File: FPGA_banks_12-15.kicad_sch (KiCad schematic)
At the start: 1 part, among them U1 XC7K410T-2FFG900I

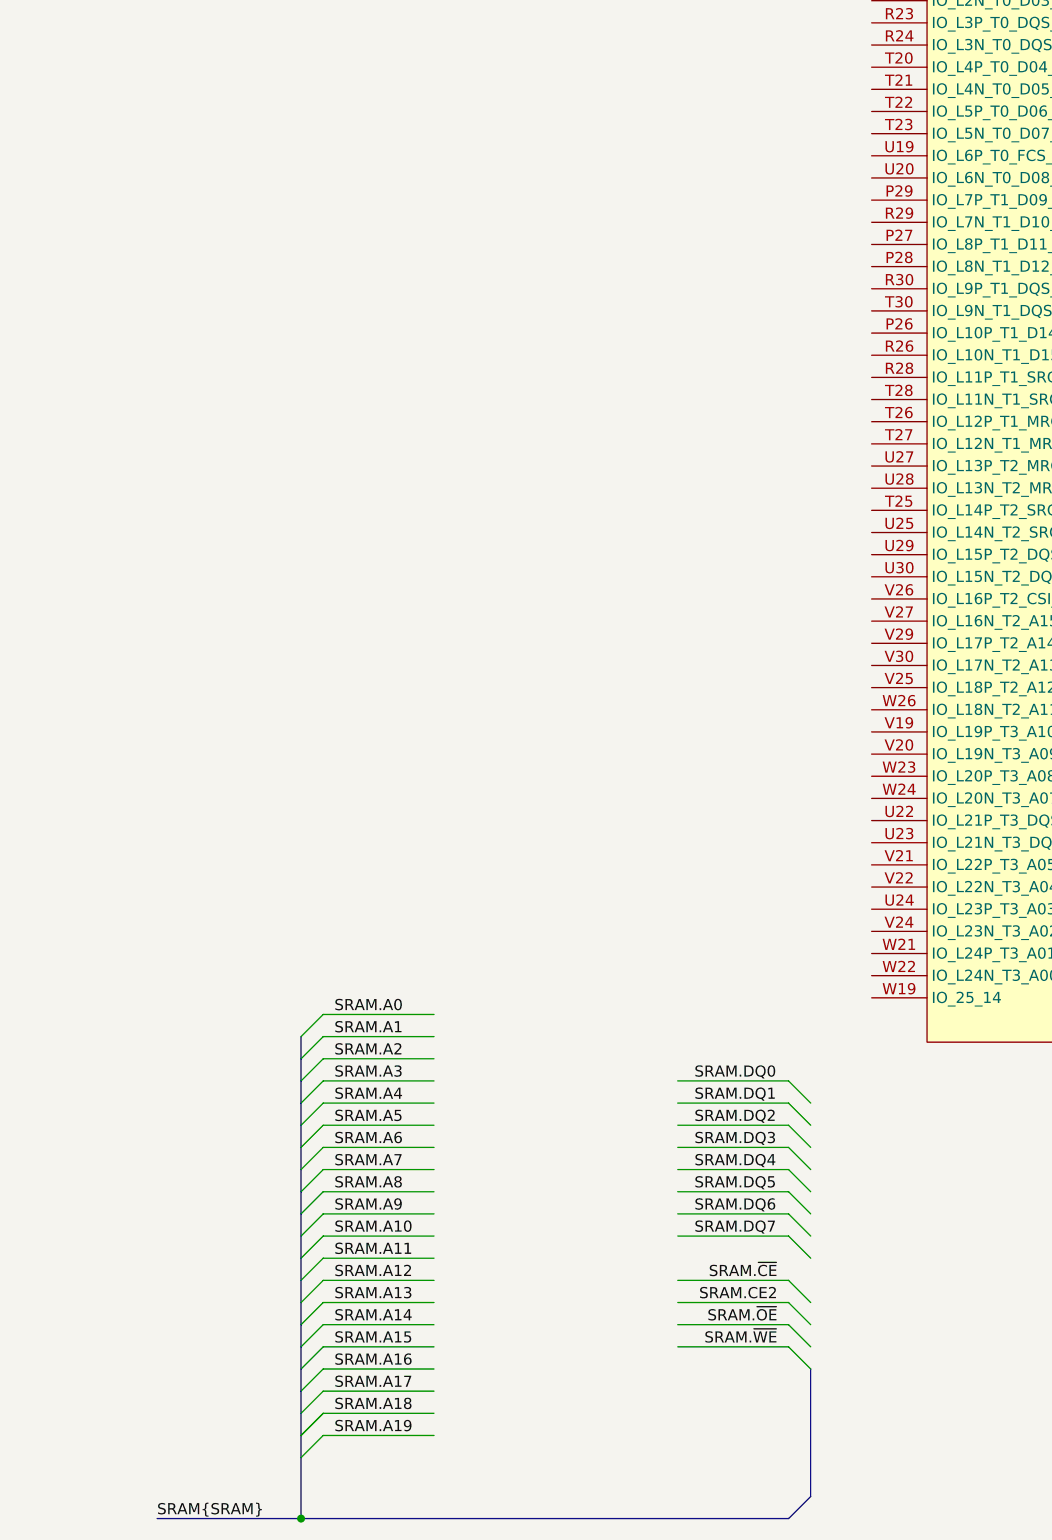
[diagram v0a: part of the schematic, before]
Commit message: Connect SRAM to FPGA
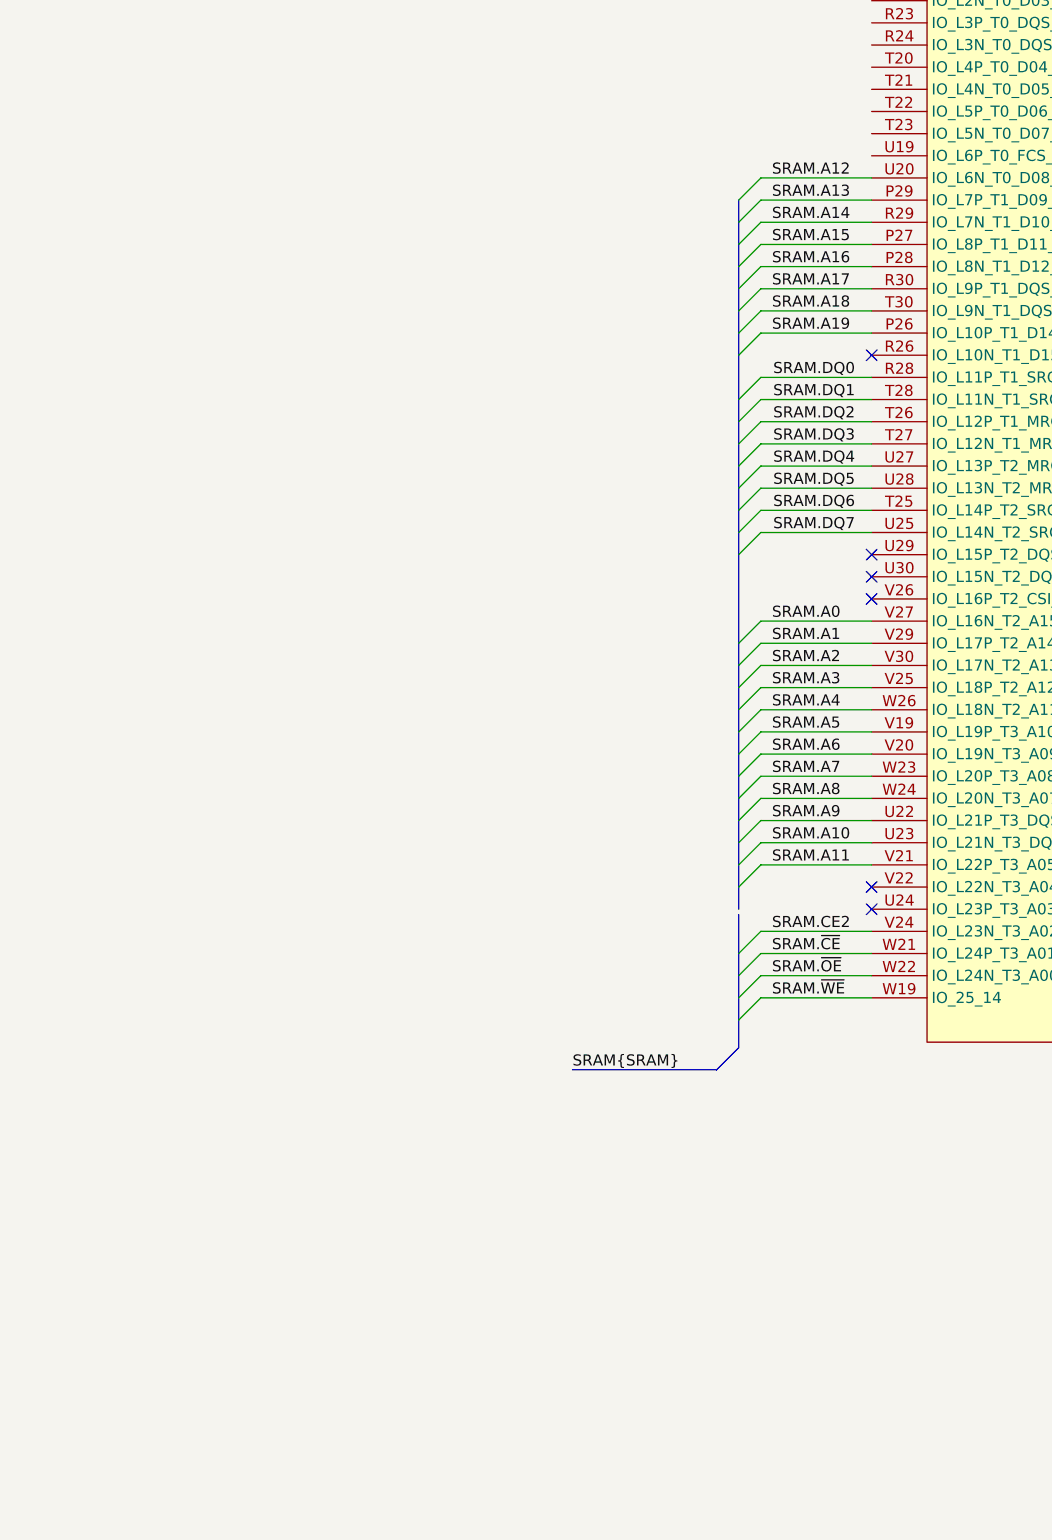
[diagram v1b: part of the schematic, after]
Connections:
- net SRAM.A0: now also U1.V27 (IO_L16N_T2_A15_D31_14)
- net SRAM.A1: now also U1.V29 (IO_L17P_T2_A14_D30_14)
- net SRAM.A10: now also U1.U23 (IO_L21N_T3_DQS_A06_D22_14)
- net SRAM.A11: now also U1.V21 (IO_L22P_T3_A05_D21_14)
- net SRAM.A12: now also U1.U20 (IO_L6N_T0_D08_VREF_14)
- net SRAM.A13: now also U1.P29 (IO_L7P_T1_D09_14)
- net SRAM.A14: now also U1.R29 (IO_L7N_T1_D10_14)
- net SRAM.A15: now also U1.P27 (IO_L8P_T1_D11_14)
- net SRAM.A16: now also U1.P28 (IO_L8N_T1_D12_14)
- net SRAM.A17: now also U1.R30 (IO_L9P_T1_DQS_14)
- net SRAM.A18: now also U1.T30 (IO_L9N_T1_DQS_D13_14)
- net SRAM.A19: now also U1.P26 (IO_L10P_T1_D14_14)
- net SRAM.A2: now also U1.V30 (IO_L17N_T2_A13_D29_14)
- net SRAM.A3: now also U1.V25 (IO_L18P_T2_A12_D28_14)
- net SRAM.A4: now also U1.W26 (IO_L18N_T2_A11_D27_14)
- net SRAM.A5: now also U1.V19 (IO_L19P_T3_A10_D26_14)
- net SRAM.A6: now also U1.V20 (IO_L19N_T3_A09_D25_VREF_14)
- net SRAM.A7: now also U1.W23 (IO_L20P_T3_A08_D24_14)
- net SRAM.A8: now also U1.W24 (IO_L20N_T3_A07_D23_14)
- net SRAM.A9: now also U1.U22 (IO_L21P_T3_DQS_14)
- net SRAM.CE2: now also U1.V24 (IO_L23N_T3_A02_D18_14)
- net SRAM.DQ0: now also U1.R28 (IO_L11P_T1_SRCC_14)
- net SRAM.DQ1: now also U1.T28 (IO_L11N_T1_SRCC_14)
- net SRAM.DQ2: now also U1.T26 (IO_L12P_T1_MRCC_14)
- net SRAM.DQ3: now also U1.T27 (IO_L12N_T1_MRCC_14)
- net SRAM.DQ4: now also U1.U27 (IO_L13P_T2_MRCC_14)
- net SRAM.DQ5: now also U1.U28 (IO_L13N_T2_MRCC_14)
- net SRAM.DQ6: now also U1.T25 (IO_L14P_T2_SRCC_14)
- net SRAM.DQ7: now also U1.U25 (IO_L14N_T2_SRCC_14)
- net SRAM.~{CE}: now also U1.W21 (IO_L24P_T3_A01_D17_14)
- net SRAM.~{OE}: now also U1.W22 (IO_L24N_T3_A00_D16_14)
- net SRAM.~{WE}: now also U1.W19 (IO_25_14)
- no-connect marks 0 -> 6

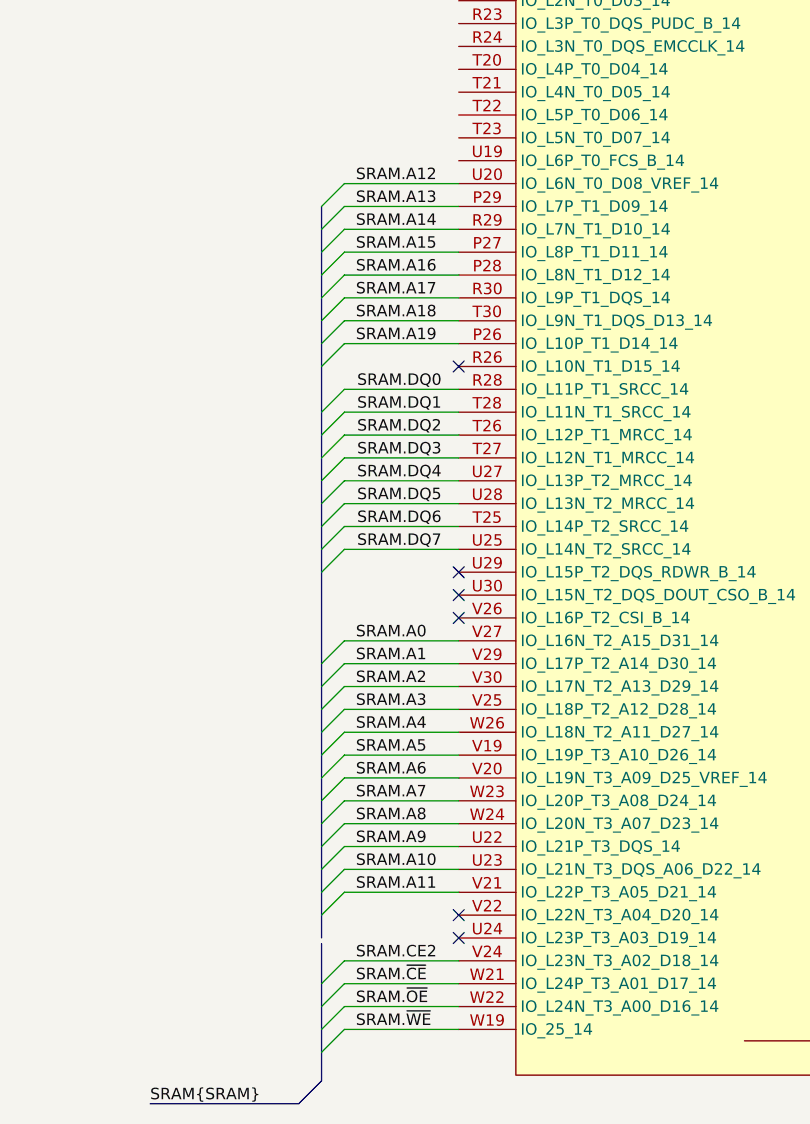
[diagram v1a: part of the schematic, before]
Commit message: Reorder SRAM singal connections to FPGA
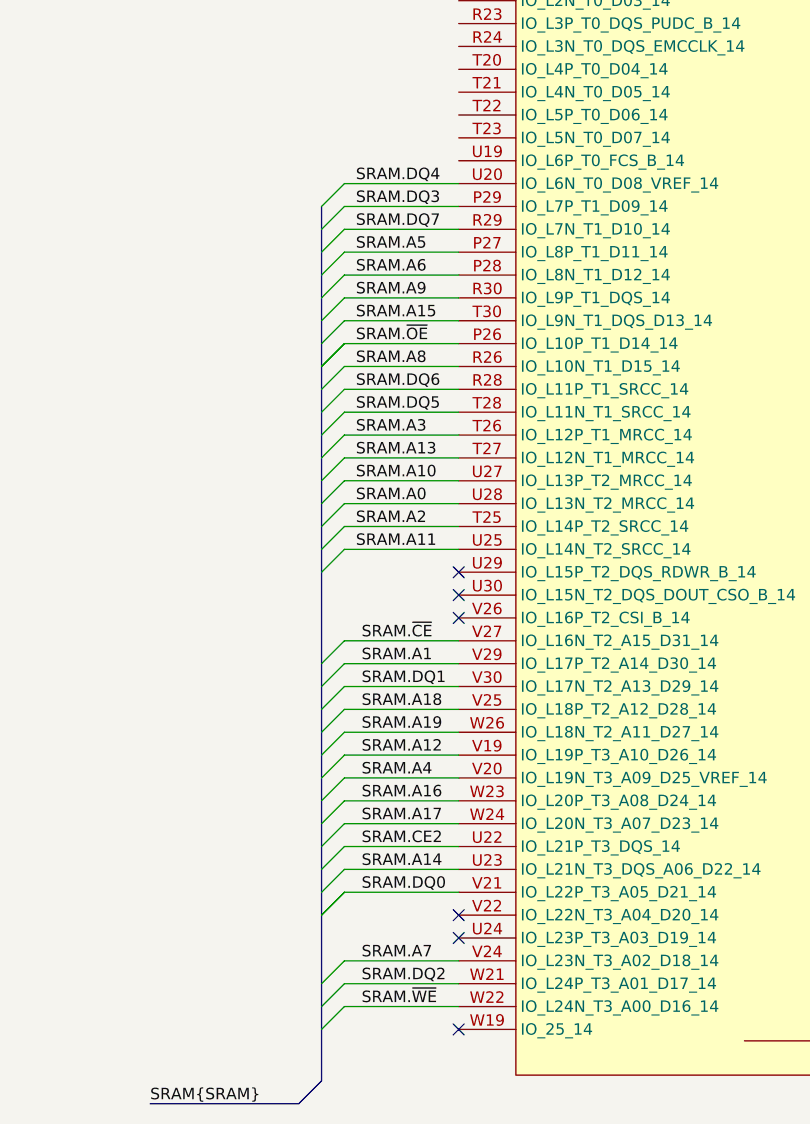
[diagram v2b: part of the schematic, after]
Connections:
- net SRAM.A0: now also U1.U28 (IO_L13N_T2_MRCC_14); no longer U1.V27 (IO_L16N_T2_A15_D31_14)
- net SRAM.A10: now also U1.U27 (IO_L13P_T2_MRCC_14); no longer U1.U23 (IO_L21N_T3_DQS_A06_D22_14)
- net SRAM.A11: now also U1.U25 (IO_L14N_T2_SRCC_14); no longer U1.V21 (IO_L22P_T3_A05_D21_14)
- net SRAM.A12: now also U1.V19 (IO_L19P_T3_A10_D26_14); no longer U1.U20 (IO_L6N_T0_D08_VREF_14)
- net SRAM.A13: now also U1.T27 (IO_L12N_T1_MRCC_14); no longer U1.P29 (IO_L7P_T1_D09_14)
- net SRAM.A14: now also U1.U23 (IO_L21N_T3_DQS_A06_D22_14); no longer U1.R29 (IO_L7N_T1_D10_14)
- net SRAM.A15: now also U1.T30 (IO_L9N_T1_DQS_D13_14); no longer U1.P27 (IO_L8P_T1_D11_14)
- net SRAM.A16: now also U1.W23 (IO_L20P_T3_A08_D24_14); no longer U1.P28 (IO_L8N_T1_D12_14)
- net SRAM.A17: now also U1.W24 (IO_L20N_T3_A07_D23_14); no longer U1.R30 (IO_L9P_T1_DQS_14)
- net SRAM.A18: now also U1.V25 (IO_L18P_T2_A12_D28_14); no longer U1.T30 (IO_L9N_T1_DQS_D13_14)
- net SRAM.A19: now also U1.W26 (IO_L18N_T2_A11_D27_14); no longer U1.P26 (IO_L10P_T1_D14_14)
- net SRAM.A2: now also U1.T25 (IO_L14P_T2_SRCC_14); no longer U1.V30 (IO_L17N_T2_A13_D29_14)
- net SRAM.A3: now also U1.T26 (IO_L12P_T1_MRCC_14); no longer U1.V25 (IO_L18P_T2_A12_D28_14)
- net SRAM.A4: now also U1.V20 (IO_L19N_T3_A09_D25_VREF_14); no longer U1.W26 (IO_L18N_T2_A11_D27_14)
- net SRAM.A5: now also U1.P27 (IO_L8P_T1_D11_14); no longer U1.V19 (IO_L19P_T3_A10_D26_14)
- net SRAM.A6: now also U1.P28 (IO_L8N_T1_D12_14); no longer U1.V20 (IO_L19N_T3_A09_D25_VREF_14)
- net SRAM.A7: now also U1.V24 (IO_L23N_T3_A02_D18_14); no longer U1.W23 (IO_L20P_T3_A08_D24_14)
- net SRAM.A8: now also U1.R26 (IO_L10N_T1_D15_14); no longer U1.W24 (IO_L20N_T3_A07_D23_14)
- net SRAM.A9: now also U1.R30 (IO_L9P_T1_DQS_14); no longer U1.U22 (IO_L21P_T3_DQS_14)
- net SRAM.CE2: now also U1.U22 (IO_L21P_T3_DQS_14); no longer U1.V24 (IO_L23N_T3_A02_D18_14)
- net SRAM.DQ0: now also U1.V21 (IO_L22P_T3_A05_D21_14); no longer U1.R28 (IO_L11P_T1_SRCC_14)
- net SRAM.DQ1: now also U1.V30 (IO_L17N_T2_A13_D29_14); no longer U1.T28 (IO_L11N_T1_SRCC_14)
- net SRAM.DQ2: now also U1.W21 (IO_L24P_T3_A01_D17_14); no longer U1.T26 (IO_L12P_T1_MRCC_14)
- net SRAM.DQ3: now also U1.P29 (IO_L7P_T1_D09_14); no longer U1.T27 (IO_L12N_T1_MRCC_14)
- net SRAM.DQ4: now also U1.U20 (IO_L6N_T0_D08_VREF_14); no longer U1.U27 (IO_L13P_T2_MRCC_14)
- net SRAM.DQ5: now also U1.T28 (IO_L11N_T1_SRCC_14); no longer U1.U28 (IO_L13N_T2_MRCC_14)
- net SRAM.DQ6: now also U1.R28 (IO_L11P_T1_SRCC_14); no longer U1.T25 (IO_L14P_T2_SRCC_14)
- net SRAM.DQ7: now also U1.R29 (IO_L7N_T1_D10_14); no longer U1.U25 (IO_L14N_T2_SRCC_14)
- net SRAM.~{CE}: now also U1.V27 (IO_L16N_T2_A15_D31_14); no longer U1.W21 (IO_L24P_T3_A01_D17_14)
- net SRAM.~{OE}: now also U1.P26 (IO_L10P_T1_D14_14); no longer U1.W22 (IO_L24N_T3_A00_D16_14)
- net SRAM.~{WE}: now also U1.W22 (IO_L24N_T3_A00_D16_14); no longer U1.W19 (IO_25_14)

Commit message: Unify title block
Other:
- title: (none) -> K410T devboard
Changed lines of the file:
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@@
   (paper "A3")
   (title_block
-    (comment 1 "www.antmicro.com")
-    (comment 2 "Antmicro Ltd")
+    (title "K410T devboard")
+    (date "2022-12-20")
+    (rev "0.0.99")
   )
   (no_connect (at 255.27 187.96))
